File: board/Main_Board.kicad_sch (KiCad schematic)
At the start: 15 parts, among them SW1 SW_SPDT, U1 Teensy4.1_DEV-16771

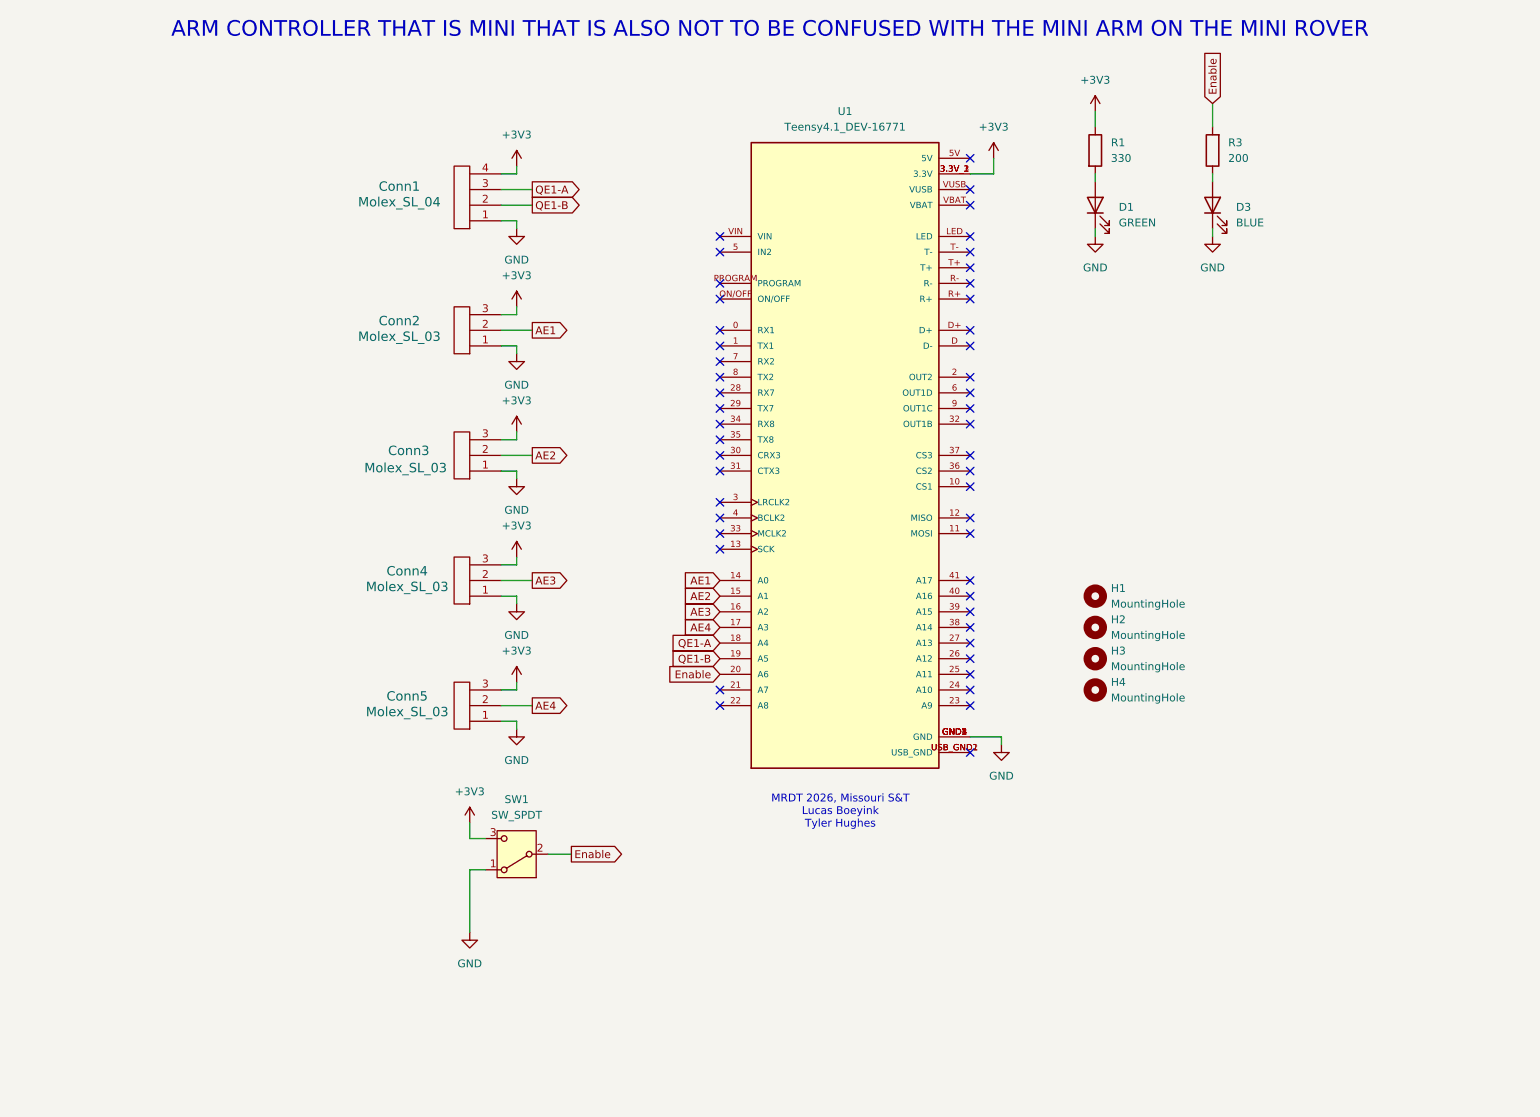
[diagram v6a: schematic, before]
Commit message: add I2C bus, reverted encoder breakout
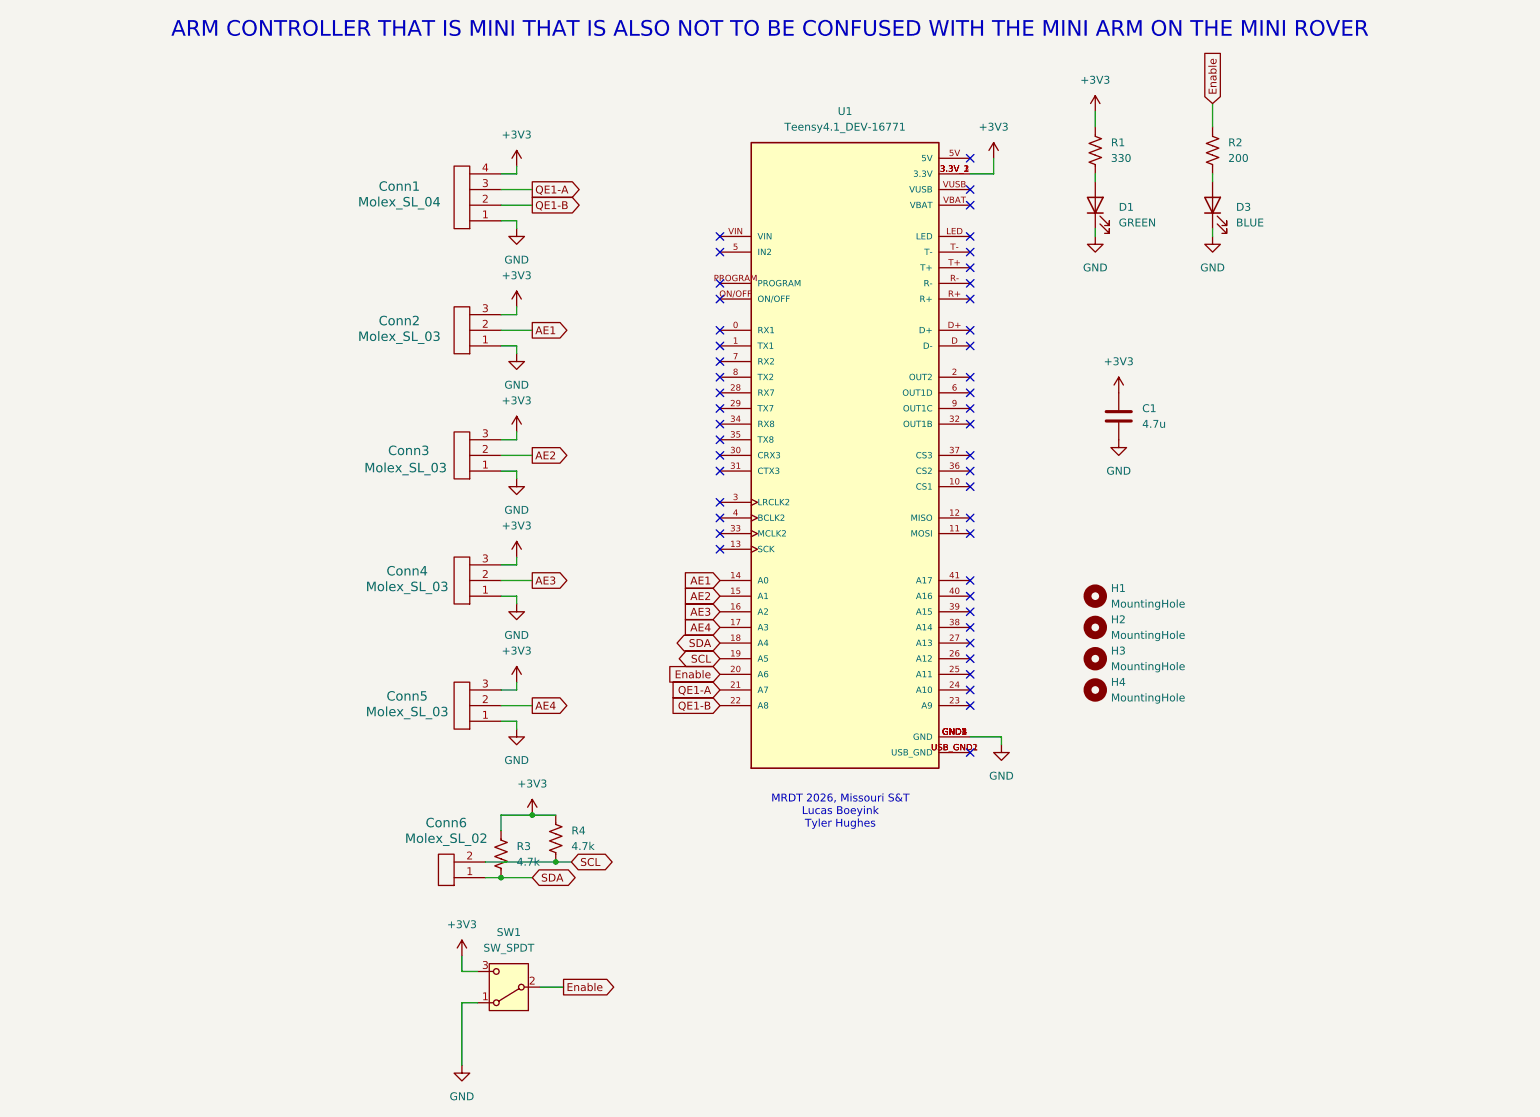
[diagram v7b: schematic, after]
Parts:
- removed R1: 330, Resistor_SMD:R_0603_1608Metric_Pad0.98x0.95mm_HandSolder, symbol Device:R
- removed R3: 200, Resistor_SMD:R_0603_1608Metric_Pad0.98x0.95mm_HandSolder, symbol Device:R
- added C1: 4.7u, symbol Device:C
- added Conn6: Molex_SL_02, symbol MRDT_Connectors:Molex_SL_02
- added R1: 330, symbol Device:R_US
- added R2: 200, symbol Device:R_US
- added R3, R4: 4.7k, symbol Device:R_US
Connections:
- net +3V3: now also C1.1, R1.1, R3.1, R4.1
- net Enable: now also R2.1
- net GND: now also C1.2
- net QE1-A: now also U1.21 (A7); no longer U1.18 (A4)
- net QE1-B: now also U1.22 (A8); no longer U1.19 (A5)
- net at D3.2 (A): now also R2.2
- net at D1.2 (A): now also R1.2
- new net SCL: Conn6.2, R4.2, U1.19 (A5)
- new net SDA: Conn6.1, R3.2, U1.18 (A4)
- no-connect marks 49 -> 47
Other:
- moved on the sheet: SW1

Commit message: Add main board general layout
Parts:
- removed Conn1: Molex_SL_04, Connector_JST:JST_PH_B4B-PH-K_1x04_P2.00mm_Vertical, symbol MRDT_Connectors:Molex_SL_04
- removed Conn2, Conn3, Conn4, Conn5: Molex_SL_03, Connector_JST:JST_PH_B3B-PH-K_1x03_P2.00mm_Vertical, symbol MRDT_Connectors:Molex_SL_03
- removed Conn6: Molex_SL_02, symbol MRDT_Connectors:Molex_SL_02
- added J1: X Axis Encoder, Connector_JST:JST_PH_B4B-PH-K_1x04_P2.00mm_Vertical, symbol Connector:Conn_01x04_Pin
- added J2: J2 Encoder, Connector_JST:JST_PH_B3B-PH-K_1x03_P2.00mm_Vertical, symbol Connector:Conn_01x03_Pin
- added J3: J3 Encoder, Connector_JST:JST_PH_B3B-PH-K_1x03_P2.00mm_Vertical, symbol Connector:Conn_01x03_Pin
- added J4: J4 Encoder, Connector_JST:JST_PH_B3B-PH-K_1x03_P2.00mm_Vertical, symbol Connector:Conn_01x03_Pin
- added J5: Pitch Encoder, Connector_JST:JST_PH_B3B-PH-K_1x03_P2.00mm_Vertical, symbol Connector:Conn_01x03_Pin
- added J6: I2C Bus, Connector_JST:JST_PH_B2B-PH-K_1x02_P2.00mm_Vertical, symbol Connector:Conn_01x02_Pin
- C1: footprint (none) -> Capacitor_SMD:C_0603_1608Metric_Pad1.08x0.95mm_HandSolder
- H1, H2, H4: footprint (none) -> MRDT_Drill_Holes:4_40_Hole
- H3: footprint MountingHole:MountingHole_4.3mm_M4_ISO14580_Pad_TopBottom -> MRDT_Drill_Holes:4_40_Hole
- R1, R2, R3, R4: footprint (none) -> Resistor_SMD:R_0603_1608Metric_Pad0.98x0.95mm_HandSolder
- SW1: value SW_SPDT -> Enable Switch
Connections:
- net +3V3: now also J1.1 (Pin_1), J2.1 (Pin_1), J3.1 (Pin_1), J4.1 (Pin_1), J5.1 (Pin_1)
- net AE1: now also J2.2 (Pin_2)
- net AE2: now also J3.2 (Pin_2)
- net AE3: now also J4.2 (Pin_2)
- net AE4: now also J5.2 (Pin_2)
- net GND: now also J1.4 (Pin_4), J2.3 (Pin_3), J3.3 (Pin_3), J4.3 (Pin_3), J5.3 (Pin_3)
- net QE1-A: now also J1.2 (Pin_2)
- net QE1-B: now also J1.3 (Pin_3)
- net SCL: now also J6.1 (Pin_1)
- net SDA: now also J6.2 (Pin_2)
